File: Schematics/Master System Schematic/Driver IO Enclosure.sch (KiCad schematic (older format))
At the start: 6 parts, among them U11 CAN_Bus_Module, U12 KY-019

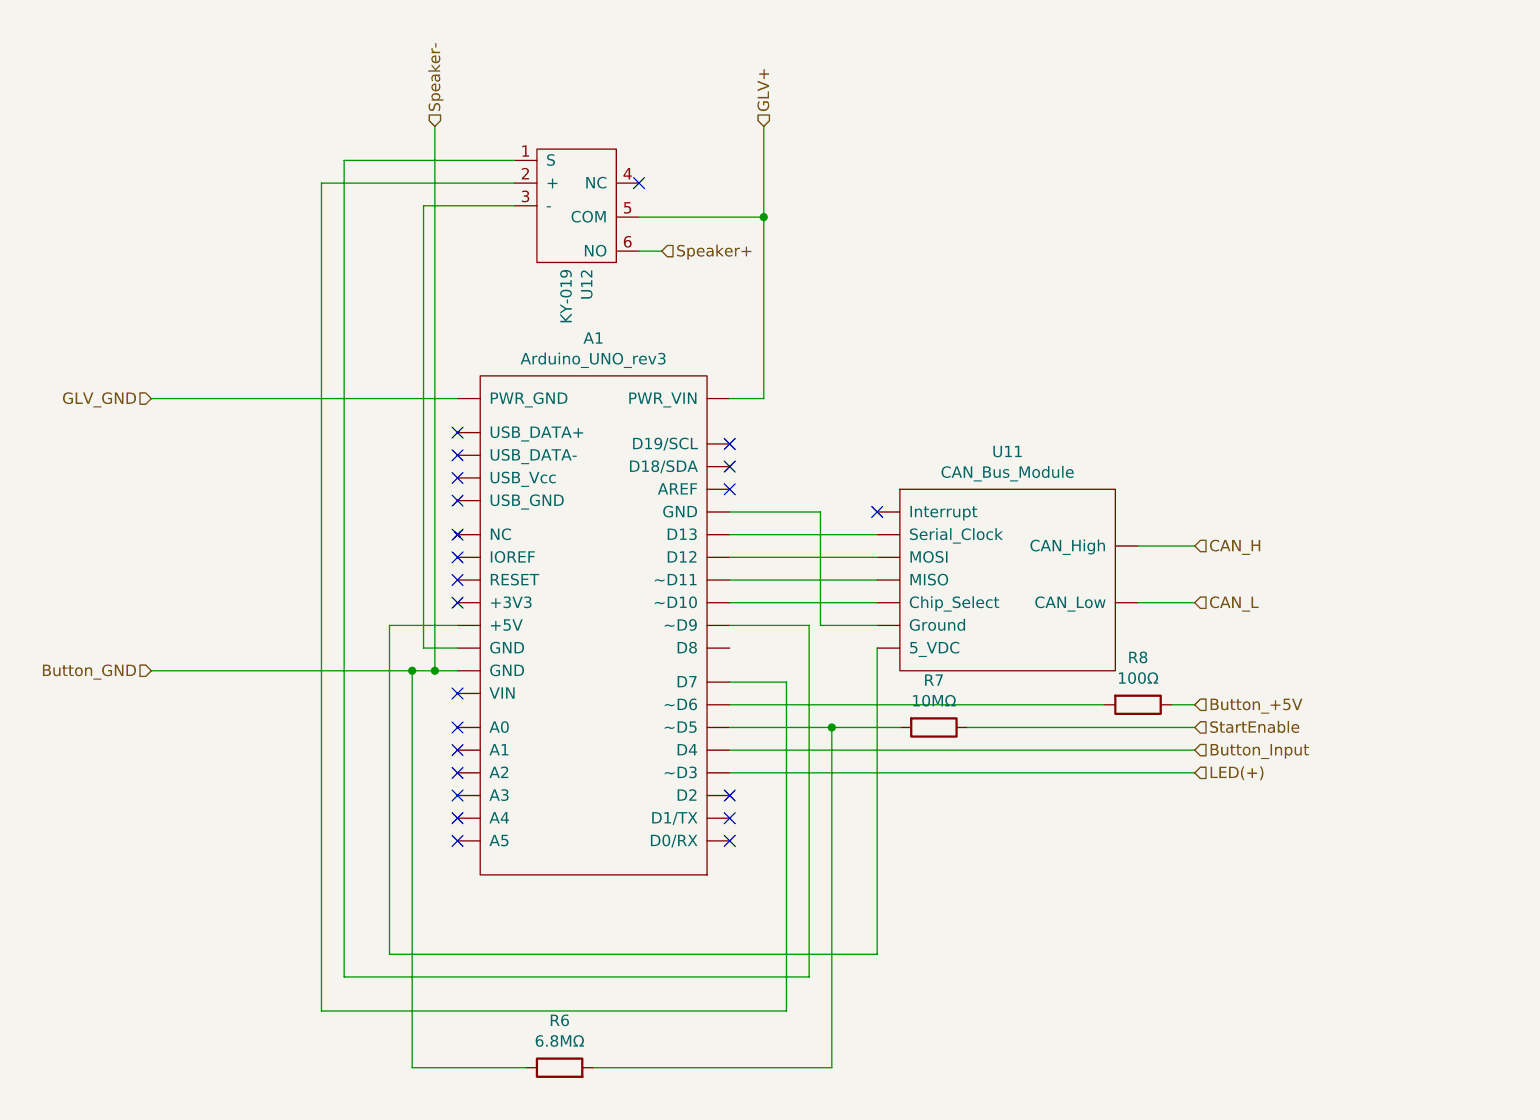
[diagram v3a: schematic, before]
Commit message: Fixed Arduino wiring
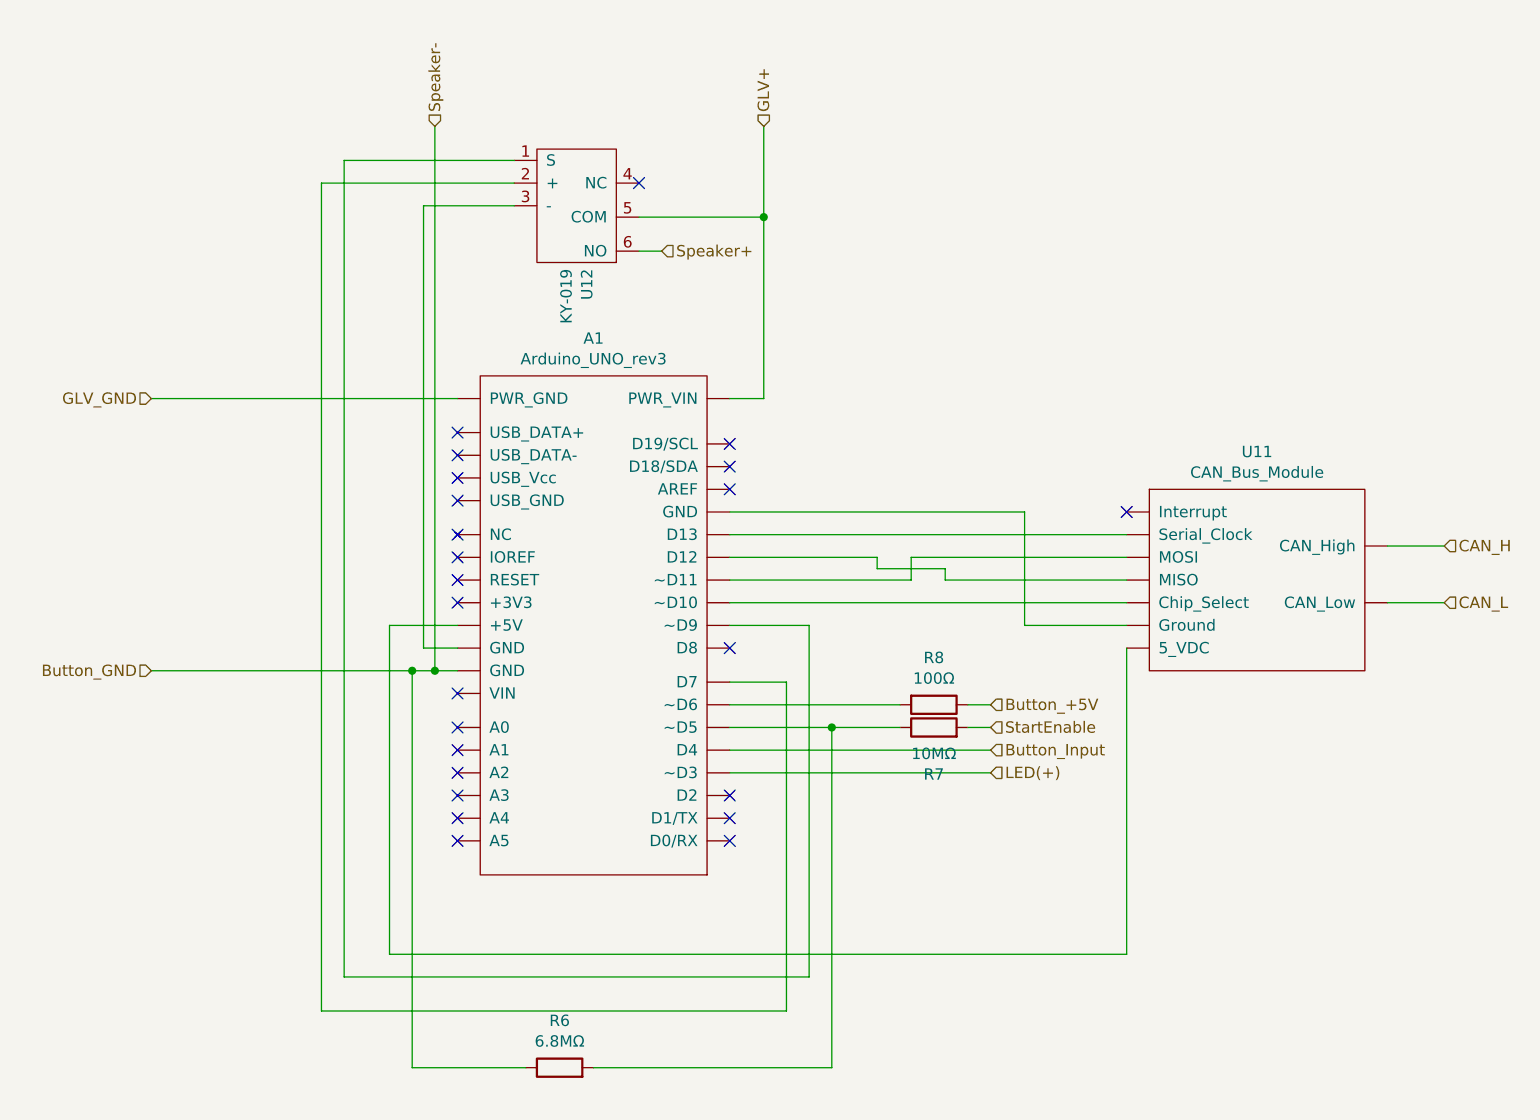
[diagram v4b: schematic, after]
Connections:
- net StartEnable: now also R7.2; no longer R7.1
- new net: A1.~ (~~D9), U11.~ (Serial_Clock) (x6)
- new net: A1.~ (~~D9), R6.2, R7.1
- no-connect marks 23 -> 24
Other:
- moved on the sheet: R8, U11
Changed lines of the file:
@@
 	4750 1750 4750 4150
-Wire Wire Line
-	6700 5400 4550 5400
 Wire Wire Line
 	4550 5400 4550 3950
@@
 NoConn ~ 6050 3250
 NoConn ~ 6050 3350
-Text HLabel 8100 4600 2    50   Input ~ 0
+Text HLabel 7200 4600 2    50   Input ~ 0
 LED(+)
 Wire Wire Line
@@
 Text HLabel 3500 4150 0    50   Input ~ 0
 Button_GND
-Text HLabel 8100 4500 2    50   Input ~ 0
+Text HLabel 7200 4500 2    50   Input ~ 0
 Button_Input
-Text HLabel 8100 4300 2    50   Input ~ 0
+Text HLabel 7200 4300 2    50   Input ~ 0
 Button_+5V
 Text HLabel 5750 2300 2    50   Input ~ 0
@@
 L Device:R R8
 U 1 1 5F8E0B40
-P 7850 4300
-F 0 "R8" V 7643 4300 50  0000 C CNN
-F 1 "100Ω" V 7734 4300 50  0000 C CNN
-F 2 "" V 7780 4300 50  0001 C CNN
-F 3 "~" H 7850 4300 50  0001 C CNN
-	1    7850 4300
+P 6950 4300
+F 0 "R8" V 6743 4300 50  0000 C CNN
+F 1 "100Ω" V 6834 4300 50  0000 C CNN
+F 2 "" V 6880 4300 50  0001 C CNN
+F 3 "~" H 6950 4300 50  0001 C CNN
+	1    6950 4300
 	0    1    1    0
 $EndComp
+NoConn ~ 7800 3450
 Wire Wire Line
-	8000 4300 8100 4300
-NoConn ~ 6700 3450
-Wire Wire Line
-	8100 3600 7850 3600
-Text HLabel 8100 3600 2    50   Input ~ 0
+	9200 3600 8950 3600
+Text HLabel 9200 3600 2    50   Input ~ 0
 CAN_H
 Wire Wire Line
-	8100 3850 7850 3850
-Text HLabel 8100 3850 2    50   Input ~ 0
+	9200 3850 8950 3850
+Text HLabel 9200 3850 2    50   Input ~ 0
 CAN_L
 $Comp
 L NER:CAN_Bus_Module U11
 U 1 1 5F847676
-P 7250 3300
-F 0 "U11" H 7275 3415 50  0000 C CNN
-F 1 "CAN_Bus_Module" H 7275 3324 50  0000 C CNN
-F 2 "" H 7250 3300 50  0001 C CNN
-F 3 "" H 7250 3300 50  0001 C CNN
-	1    7250 3300
+P 8350 3300
+F 0 "U11" H 8375 3415 50  0000 C CNN
+F 1 "CAN_Bus_Module" H 8375 3324 50  0000 C CNN
+F 2 "" H 8350 3300 50  0001 C CNN
+F 3 "" H 8350 3300 50  0001 C CNN
+	1    8350 3300
 	1    0    0    -1
 $EndComp
@@
 F 3 "~" H 6950 4400 50  0001 C CNN
 	1    6950 4400
-	0    1    1    0
+	0    -1   -1   0
 $EndComp
-Text HLabel 8100 4400 2    50   Input ~ 0
+Text HLabel 7200 4400 2    50   Input ~ 0
 StartEnable
 Wire Wire Line
@@
 	6500 4400 6800 4400
 Wire Wire Line
-	6050 3850 6700 3850
-Wire Wire Line
-	6050 3750 6700 3750
-Wire Wire Line
-	6050 3650 6700 3650
-Wire Wire Line
-	6050 3550 6700 3550
-Wire Wire Line
-	6700 3950 6450 3950
-Wire Wire Line
-	6450 3950 6450 3450
-Wire Wire Line
-	6450 3450 6050 3450
-Wire Wire Line
-	7100 4400 8100 4400
-Wire Wire Line
-	6050 4500 8100 4500
-Wire Wire Line
-	6050 4600 8100 4600
-Wire Wire Line
-	6700 4050 6700 5400
-Wire Wire Line
-	7700 4300 6050 4300
-Wire Wire Line
 	6200 1750 6200 2150
 Wire Wire Line
 	3500 2950 4850 2950
+Wire Wire Line
+	6800 4300 6050 4300
+Wire Wire Line
+	6050 4500 7200 4500
+Wire Wire Line
+	7200 4600 6050 4600
+Wire Wire Line
+	7200 4300 7100 4300
+Wire Wire Line
+	7100 4400 7200 4400
+Wire Wire Line
+	6050 3850 7800 3850
+Wire Wire Line
+	7800 3650 6850 3650
+Wire Wire Line
+	6850 3650 6850 3750
+Wire Wire Line
+	6850 3750 6050 3750
+Wire Wire Line
+	7800 3550 6050 3550
+Wire Wire Line
+	7800 3750 7000 3750
+Wire Wire Line
+	7000 3700 7000 3750
+Wire Wire Line
+	6700 3700 6700 3650
+Wire Wire Line
+	6700 3650 6050 3650
+Wire Wire Line
+	6700 3700 7000 3700
+Wire Wire Line
+	7350 3450 7350 3950
+Wire Wire Line
+	7350 3950 7800 3950
+Wire Wire Line
+	6050 3450 7350 3450
+Wire Wire Line
+	7800 4050 7800 5400
+Wire Wire Line
+	4550 5400 7800 5400
+NoConn ~ 6050 4050
 $EndSCHEMATC

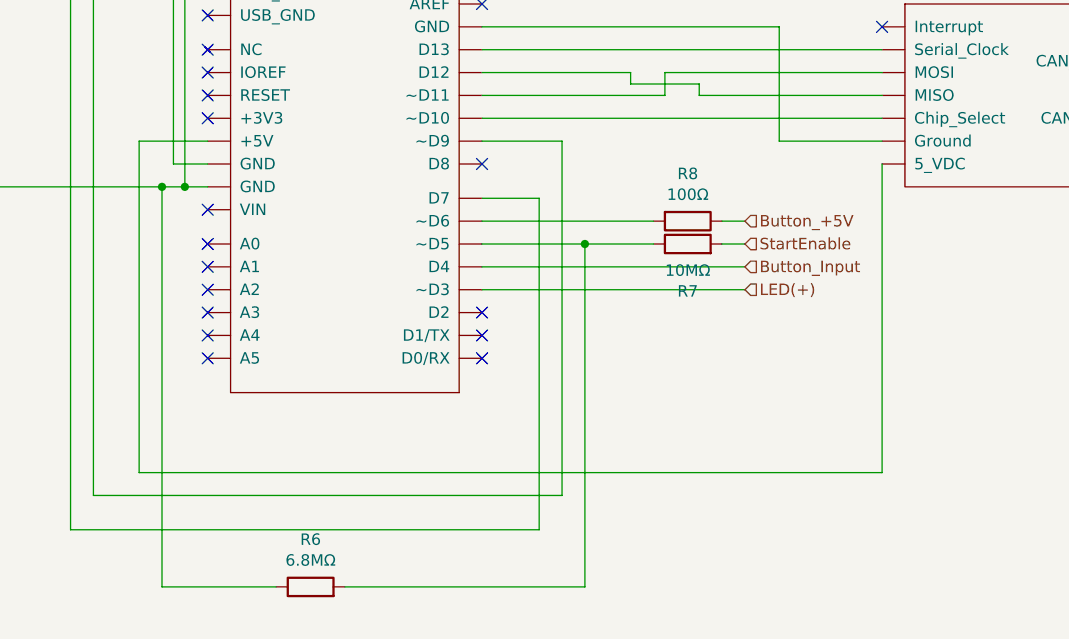
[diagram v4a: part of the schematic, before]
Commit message: Fixed Driver IO LED Voltage Divider
Added voltage divider to LED to bring 5v down to 3v.
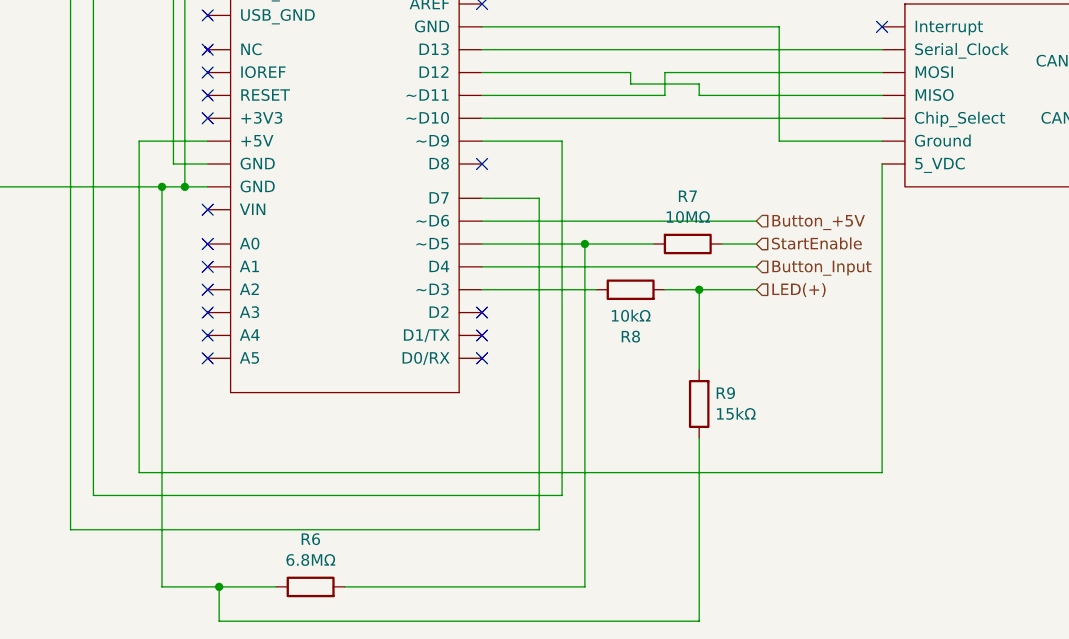
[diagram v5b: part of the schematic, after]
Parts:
- added R9: 15kΩ, symbol Device:R
- R8: value 100Ω -> 10kΩ
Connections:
- net Button_+5V: now also A1.~ (~~D9); no longer R8.1
- net Button_GND: now also R9.1
- net LED(+): now also R8.2, R9.2; no longer A1.~ (~~D9)
- net StartEnable: now also R7.1; no longer R7.2
- new net: A1.~ (~~D9), U11.~ (Serial_Clock) (x6)
- new net: A1.~ (~~D9), R6.2, R7.2
- new net: A1.~ (~~D9), R8.1
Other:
- moved on the sheet: R8
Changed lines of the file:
@@
 EESchema Schematic File Version 4
-LIBS:Master System Schematic-cache
 EELAYER 30 0
 EELAYER END
@@
 NoConn ~ 6050 3250
 NoConn ~ 6050 3350
-Text HLabel 7200 4600 2    50   Input ~ 0
+Text HLabel 7250 4600 2    50   Input ~ 0
 LED(+)
 Wire Wire Line
@@
 Text HLabel 3500 4150 0    50   Input ~ 0
 Button_GND
-Text HLabel 7200 4500 2    50   Input ~ 0
+Text HLabel 7250 4500 2    50   Input ~ 0
 Button_Input
-Text HLabel 7200 4300 2    50   Input ~ 0
+Text HLabel 7250 4300 2    50   Input ~ 0
 Button_+5V
 Text HLabel 5750 2300 2    50   Input ~ 0
@@
 	4650 5900 4650 4150
 Wire Wire Line
-	4650 5900 5150 5900
+	4650 5900 4900 5900
 Connection ~ 4650 4150
 Wire Wire Line
 	4650 4150 4750 4150
-$Comp
-L Device:R R8
-U 1 1 5F8E0B40
-P 6950 4300
-F 0 "R8" V 6743 4300 50  0000 C CNN
-F 1 "100Ω" V 6834 4300 50  0000 C CNN
-F 2 "" V 6880 4300 50  0001 C CNN
-F 3 "~" H 6950 4300 50  0001 C CNN
-	1    6950 4300
-	0    1    1    0
-$EndComp
 NoConn ~ 7800 3450
 Wire Wire Line
@@
 F 3 "~" H 6950 4400 50  0001 C CNN
 	1    6950 4400
-	0    -1   -1   0
-$EndComp
-Text HLabel 7200 4400 2    50   Input ~ 0
+	0    1    1    0
+$EndComp
+Text HLabel 7250 4400 2    50   Input ~ 0
 StartEnable
 Wire Wire Line
@@
 	3500 2950 4850 2950
 Wire Wire Line
-	6800 4300 6050 4300
-Wire Wire Line
-	6050 4500 7200 4500
-Wire Wire Line
-	7200 4600 6050 4600
-Wire Wire Line
-	7200 4300 7100 4300
-Wire Wire Line
-	7100 4400 7200 4400
-Wire Wire Line
 	6050 3850 7800 3850
 Wire Wire Line
@@
 Wire Wire Line
 	7350 3450 7350 3950
-Wire Wire Line
-	7350 3950 7800 3950
 Wire Wire Line
 	6050 3450 7350 3450
@@
 	4550 5400 7800 5400
 NoConn ~ 6050 4050
+$Comp
+L Device:R R8
+U 1 1 5F8E0B40
+P 6700 4600
+F 0 "R8" V 6493 4600 50  0000 C CNN
+F 1 "10kΩ" V 6584 4600 50  0000 C CNN
+F 2 "" V 6630 4600 50  0001 C CNN
+F 3 "~" H 6700 4600 50  0001 C CNN
+	1    6700 4600
+	0    -1   -1   0
+$EndComp
+$Comp
+L Device:R R9
+U 1 1 5F8E3DF1
+P 7000 5100
+F 0 "R9" H 6930 5054 50  0000 R CNN
+F 1 "15kΩ" H 6930 5145 50  0000 R CNN
+F 2 "" V 6930 5100 50  0001 C CNN
+F 3 "~" H 7000 5100 50  0001 C CNN
+	1    7000 5100
+	-1   0    0    1
+$EndComp
+Wire Wire Line
+	7100 4400 7250 4400
+Wire Wire Line
+	6050 4500 7250 4500
+Wire Wire Line
+	7350 3950 7800 3950
+Wire Wire Line
+	6050 4300 7250 4300
+Wire Wire Line
+	6850 4600 7000 4600
+Wire Wire Line
+	6050 4600 6550 4600
+Wire Wire Line
+	7000 4600 7000 4950
+Connection ~ 7000 4600
+Wire Wire Line
+	7000 4600 7250 4600
+Wire Wire Line
+	7000 5250 7000 6050
+Wire Wire Line
+	7000 6050 4900 6050
+Wire Wire Line
+	4900 6050 4900 5900
+Connection ~ 4900 5900
+Wire Wire Line
+	4900 5900 5150 5900
 $EndSCHEMATC

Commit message: Added cooling pump off while charging functionality
>Added diode so glv battery cannot supply charging power to bms
>added pulldown resistor for charging power line to ground
>Connected charging power line to second side of cooling pump relay coil
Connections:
- new net: A1.~ (~~D9), U11.~ (Serial_Clock) (x6)
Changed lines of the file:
@@
 $Descr A4 11693 8268
 encoding utf-8
-Sheet 5 21
+Sheet 4 21
 Title ""
 Date "2020-10-12"
